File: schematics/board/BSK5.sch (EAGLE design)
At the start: 88 parts, among them U1 STM32F405RGT6, X1 JST-6, X11 JST-6

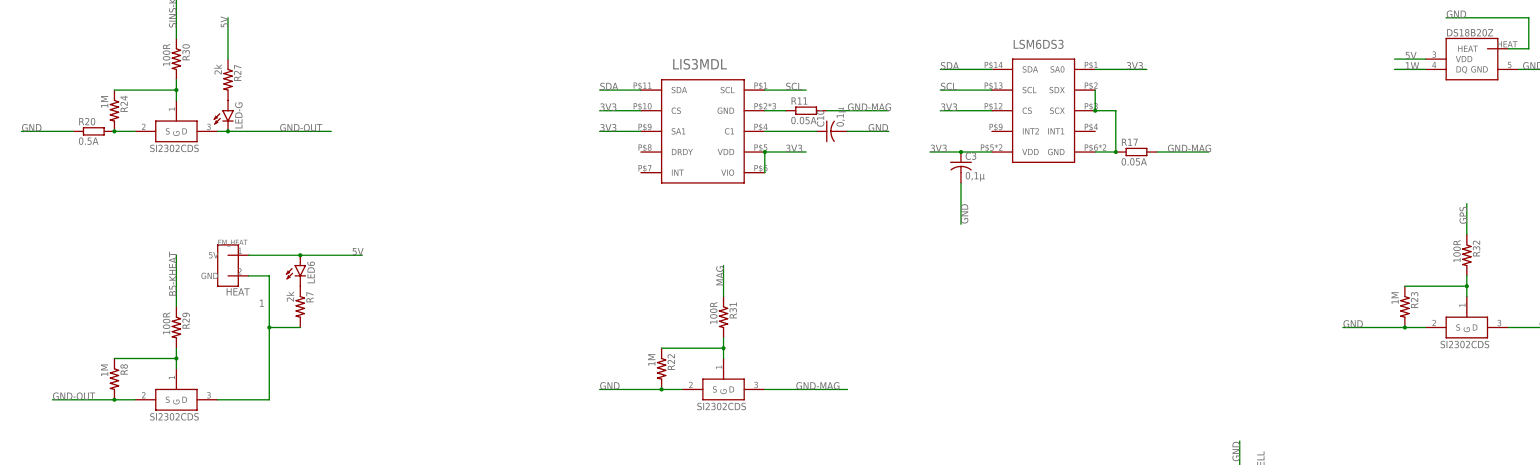
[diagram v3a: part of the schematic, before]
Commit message: На платах БСК устройства по умолчанию подтянуты к питанию
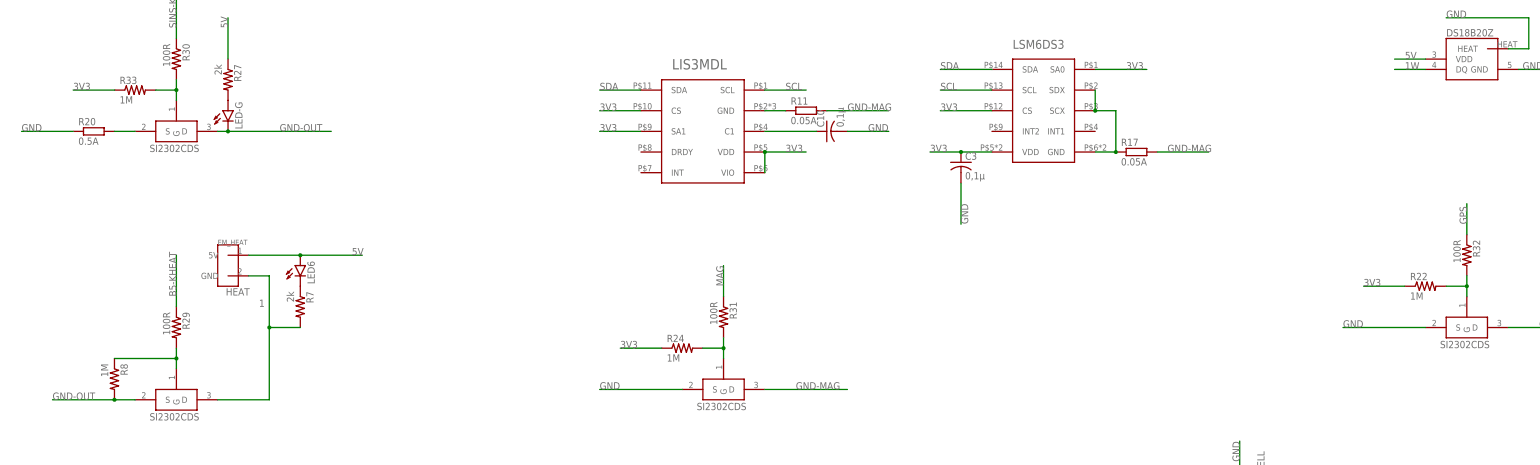
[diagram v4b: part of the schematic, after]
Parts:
- removed R23: 1M, resistor:R-US_R0603
- added R33: 1M, resistor:R-US_R0603
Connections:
- net 11: no longer R24.2
- net 3V3: now also R22.1, R24.1, R33.1
- net GND: no longer R22.2, R23.2
- net N$10: now also R33.2; no longer R24.1
- net N$11: now also R24.2; no longer R22.1
- net N$13: now also R22.2; no longer R23.1
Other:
- moved on the sheet: R22, R24
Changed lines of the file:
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@@
 <part name="R21" library="rcl" library_urn="urn:adsk.eagle:library:334" deviceset="R-EU_" device="R1210" package3d_urn="urn:adsk.eagle:package:23554/2" value="0.2A"/>
 <part name="U$19" library="CanCubeSat" deviceset="SI2302CDS" device=""/>
-<part name="R22" library="resistor" deviceset="R-US_" device="R0603" package3d_urn="urn:adsk.eagle:package:23555/3" value="1M"/>
 <part name="U$20" library="CanCubeSat" deviceset="SI2302CDS" device=""/>
-<part name="R23" library="resistor" deviceset="R-US_" device="R0603" package3d_urn="urn:adsk.eagle:package:23555/3" value="1M"/>
 <part name="U$21" library="CanCubeSat" deviceset="Q24" device=""/>
 <part name="C4" library="rcl" library_urn="urn:adsk.eagle:library:334" deviceset="C-EU" device="C0603" package3d_urn="urn:adsk.eagle:package:23616/2" value="1nF"/>
@@
 <part name="R20" library="rcl" library_urn="urn:adsk.eagle:library:334" deviceset="R-EU_" device="R1210" package3d_urn="urn:adsk.eagle:package:23554/2" value="0.5A"/>
 <part name="U$22" library="CanCubeSat" deviceset="SI2302CDS" device=""/>
-<part name="R24" library="resistor" deviceset="R-US_" device="R0603" package3d_urn="urn:adsk.eagle:package:23555/3" value="1M"/>
 <part name="R27" library="resistor" deviceset="R-US_" device="R0603" package3d_urn="urn:adsk.eagle:package:23555/3" value="2k"/>
 <part name="LED-G" library="led" library_urn="urn:adsk.eagle:library:259" deviceset="LED" device="CHIPLED_0603" package3d_urn="urn:adsk.eagle:package:15822/2"/>
@@
 <part name="R32" library="resistor" deviceset="R-US_" device="R0603" package3d_urn="urn:adsk.eagle:package:23555/3" value="100R"/>
 <part name="U$12" library="CanCubeSat" deviceset="FFC-CONNECT" device="68611"/>
+<part name="R33" library="resistor" deviceset="R-US_" device="R0603" package3d_urn="urn:adsk.eagle:package:23555/3" value="1M"/>
+<part name="R24" library="resistor" deviceset="R-US_" device="R0603" package3d_urn="urn:adsk.eagle:package:23555/3" value="1M"/>
+<part name="R22" library="resistor" deviceset="R-US_" device="R0603" package3d_urn="urn:adsk.eagle:package:23555/3" value="1M"/>
 </parts>
 <sheets>
@@
 </instance>
 <instance part="U$19" gate="G$1" x="340.36" y="269.24" smashed="yes"/>
-<instance part="R22" gate="G$1" x="325.12" y="274.32" smashed="yes" rot="R270">
-<attribute name="NAME" x="326.6186" y="278.13" size="1.778" layer="95" rot="R270"/>
-<attribute name="VALUE" x="321.818" y="278.13" size="1.778" layer="96" rot="R270"/>
-</instance>
 <instance part="U$20" gate="G$1" x="523.24" y="284.48" smashed="yes"/>
-<instance part="R23" gate="G$1" x="508" y="289.56" smashed="yes" rot="R270">
-<attribute name="NAME" x="509.4986" y="293.37" size="1.778" layer="95" rot="R270"/>
-<attribute name="VALUE" x="504.698" y="293.37" size="1.778" layer="96" rot="R270"/>
-</instance>
 <instance part="U$21" gate="G$1" x="533.4" y="111.76" smashed="yes" rot="R180">
 <attribute name="NAME" x="538.48" y="119.38" size="1.778" layer="95" rot="R180"/>
@@
 </instance>
 <instance part="U$22" gate="G$1" x="205.74" y="332.74" smashed="yes"/>
-<instance part="R24" gate="G$1" x="190.5" y="337.82" smashed="yes" rot="R270">
-<attribute name="NAME" x="191.9986" y="341.63" size="1.778" layer="95" rot="R270"/>
-<attribute name="VALUE" x="187.198" y="341.63" size="1.778" layer="96" rot="R270"/>
-</instance>
 <instance part="R27" gate="G$1" x="218.44" y="345.44" smashed="yes" rot="R270">
 <attribute name="NAME" x="219.9386" y="349.25" size="1.778" layer="95" rot="R270"/>
@@
 <attribute name="NAME" x="70.485" y="265.43" size="1.778" layer="95" rot="R90"/>
 <attribute name="VALUE" x="114.3" y="265.43" size="1.778" layer="96" rot="R90"/>
+</instance>
+<instance part="R33" gate="G$1" x="195.58" y="342.9" smashed="yes">
+<attribute name="NAME" x="191.77" y="344.3986" size="1.778" layer="95"/>
+<attribute name="VALUE" x="191.77" y="339.598" size="1.778" layer="96"/>
+</instance>
+<instance part="R24" gate="G$1" x="330.2" y="279.4" smashed="yes">
+<attribute name="NAME" x="326.39" y="280.8986" size="1.778" layer="95"/>
+<attribute name="VALUE" x="326.39" y="276.098" size="1.778" layer="96"/>
+</instance>
+<instance part="R22" gate="G$1" x="513.08" y="294.64" smashed="yes">
+<attribute name="NAME" x="509.27" y="296.1386" size="1.778" layer="95"/>
+<attribute name="VALUE" x="509.27" y="291.338" size="1.778" layer="96"/>
 </instance>
 </instances>
@@
 <segment>
 <pinref part="U$19" gate="G$1" pin="S"/>
-<wire x1="330.2" y1="269.24" x2="325.12" y2="269.24" width="0.1524" layer="91"/>
 <label x="309.88" y="269.24" size="1.778" layer="95"/>
-<pinref part="R22" gate="G$1" pin="2"/>
-<wire x1="325.12" y1="269.24" x2="309.88" y2="269.24" width="0.1524" layer="91"/>
-<junction x="325.12" y="269.24"/>
+<wire x1="330.2" y1="269.24" x2="309.88" y2="269.24" width="0.1524" layer="91"/>
 </segment>
 <segment>
 <pinref part="U$20" gate="G$1" pin="S"/>
-<wire x1="513.08" y1="284.48" x2="508" y2="284.48" width="0.1524" layer="91"/>
 <label x="492.76" y="284.48" size="1.778" layer="95"/>
-<pinref part="R23" gate="G$1" pin="2"/>
-<wire x1="508" y1="284.48" x2="492.76" y2="284.48" width="0.1524" layer="91"/>
-<junction x="508" y="284.48"/>
+<wire x1="513.08" y1="284.48" x2="492.76" y2="284.48" width="0.1524" layer="91"/>
 </segment>
 <segment>
@@
 <wire x1="195.58" y1="332.74" x2="190.5" y2="332.74" width="0.1524" layer="91"/>
 <pinref part="U$22" gate="G$1" pin="S"/>
-<pinref part="R24" gate="G$1" pin="2"/>
 <pinref part="R20" gate="G$1" pin="2"/>
-<junction x="190.5" y="332.74"/>
 </segment>
 </net>
@@
 <label x="73.66" y="248.92" size="1.778" layer="95" rot="R90"/>
 </segment>
+<segment>
+<pinref part="R33" gate="G$1" pin="1"/>
+<wire x1="190.5" y1="342.9" x2="180.34" y2="342.9" width="0.1524" layer="91"/>
+<label x="180.34" y="342.9" size="1.778" layer="95"/>
+</segment>
+<segment>
+<pinref part="R24" gate="G$1" pin="1"/>
+<wire x1="325.12" y1="279.4" x2="314.96" y2="279.4" width="0.1524" layer="91"/>
+<label x="314.96" y="279.4" size="1.778" layer="95"/>
+</segment>
+<segment>
+<pinref part="R22" gate="G$1" pin="1"/>
+<wire x1="508" y1="294.64" x2="497.84" y2="294.64" width="0.1524" layer="91"/>
+<label x="497.84" y="294.64" size="1.778" layer="95"/>
+</segment>
 </net>
 <net name="SINS-KVCC" class="0">
@@
 <pinref part="U$22" gate="G$1" pin="G"/>
 <wire x1="205.74" y1="345.44" x2="205.74" y2="342.9" width="0.1524" layer="91"/>
-<pinref part="R24" gate="G$1" pin="1"/>
+<pinref part="R33" gate="G$1" pin="2"/>
 <wire x1="205.74" y1="342.9" x2="205.74" y2="340.36" width="0.1524" layer="91"/>
-<wire x1="190.5" y1="342.9" x2="205.74" y2="342.9" width="0.1524" layer="91"/>
+<wire x1="200.66" y1="342.9" x2="205.74" y2="342.9" width="0.1524" layer="91"/>
 <junction x="205.74" y="342.9"/>
 </segment>
@@
 <pinref part="U$19" gate="G$1" pin="G"/>
 <wire x1="340.36" y1="281.94" x2="340.36" y2="279.4" width="0.1524" layer="91"/>
-<pinref part="R22" gate="G$1" pin="1"/>
+<pinref part="R24" gate="G$1" pin="2"/>
 <wire x1="340.36" y1="279.4" x2="340.36" y2="276.86" width="0.1524" layer="91"/>
-<wire x1="325.12" y1="279.4" x2="340.36" y2="279.4" width="0.1524" layer="91"/>
+<wire x1="335.28" y1="279.4" x2="340.36" y2="279.4" width="0.1524" layer="91"/>
 <junction x="340.36" y="279.4"/>
 </segment>
@@
 <net name="N$13" class="0">
 <segment>
-<pinref part="R23" gate="G$1" pin="1"/>
-<wire x1="508" y1="294.64" x2="523.24" y2="294.64" width="0.1524" layer="91"/>
 <pinref part="U$20" gate="G$1" pin="G"/>
-<wire x1="523.24" y1="294.64" x2="523.24" y2="292.1" width="0.1524" layer="91"/>
 <pinref part="R32" gate="G$1" pin="2"/>
 <wire x1="523.24" y1="297.18" x2="523.24" y2="294.64" width="0.1524" layer="91"/>
+<pinref part="R22" gate="G$1" pin="2"/>
+<wire x1="523.24" y1="294.64" x2="523.24" y2="292.1" width="0.1524" layer="91"/>
+<wire x1="518.16" y1="294.64" x2="523.24" y2="294.64" width="0.1524" layer="91"/>
 <junction x="523.24" y="294.64"/>
 </segment>

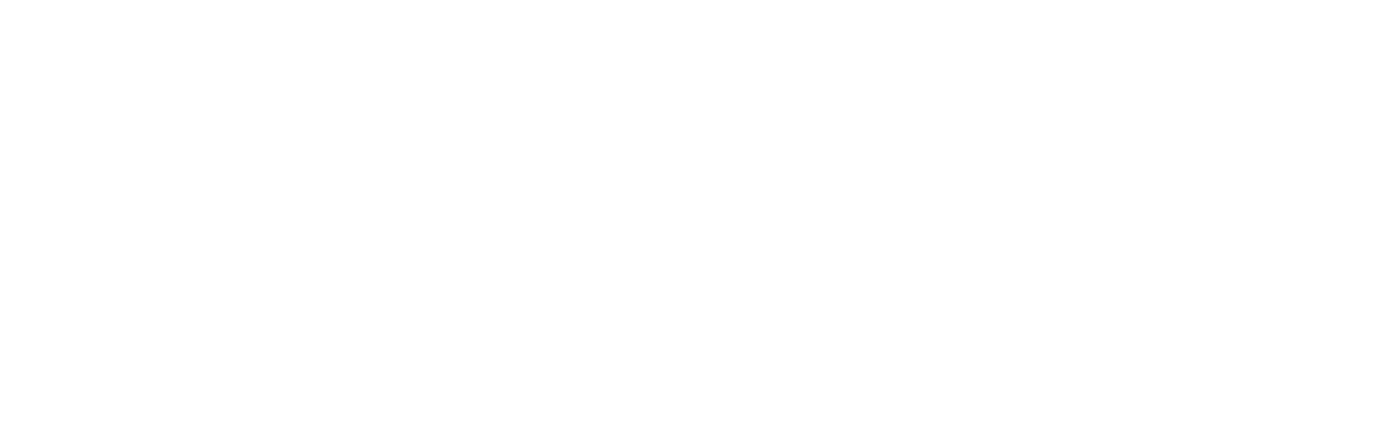
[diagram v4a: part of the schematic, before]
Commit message: Добавлены подписи Концерна к платам
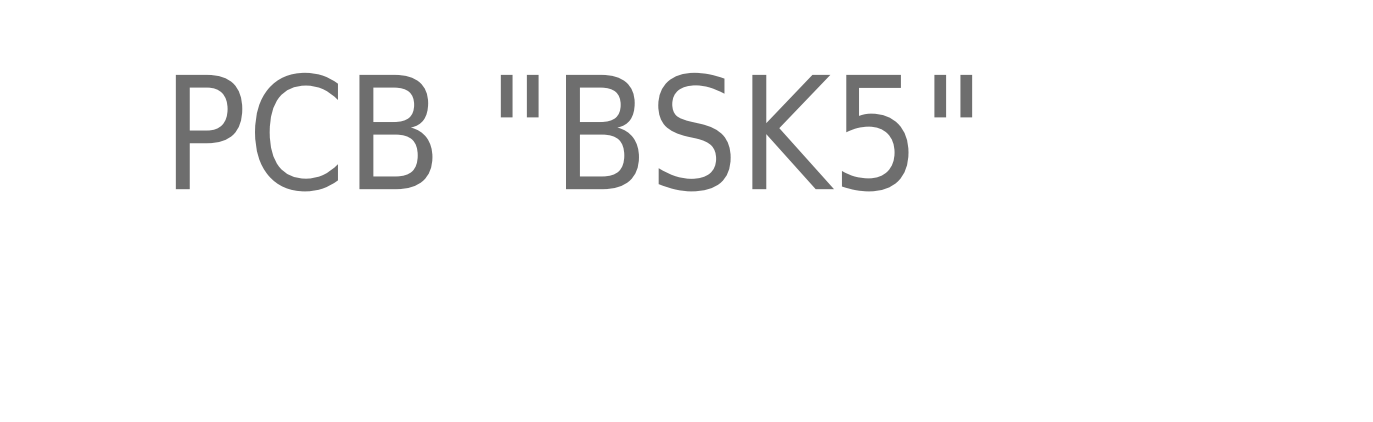
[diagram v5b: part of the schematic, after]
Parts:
- added U$26: PCB "BSK5", CanCubeSat:ITS-LOGOPCB-""
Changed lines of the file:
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@@
 <drawing>
 <settings>
-<setting alwaysvectorfont="no"/>
+<setting alwaysvectorfont="yes"/>
 <setting verticaltext="up"/>
 </settings>
@@
 <part name="R24" library="resistor" deviceset="R-US_" device="R0603" package3d_urn="urn:adsk.eagle:package:23555/3" value="1M"/>
 <part name="R22" library="resistor" deviceset="R-US_" device="R0603" package3d_urn="urn:adsk.eagle:package:23555/3" value="1M"/>
+<part name="U$26" library="CanCubeSat" deviceset="ITS-LOGO" device="PCB-&quot;&quot;" value="PCB &quot;BSK5&quot;"/>
 </parts>
 <sheets>
@@
 <attribute name="VALUE" x="509.27" y="291.338" size="1.778" layer="96"/>
 </instance>
+<instance part="U$26" gate="G$1" x="182.88" y="434.34" smashed="yes">
+<attribute name="VALUE" x="309.88" y="434.34" size="12.7" layer="96"/>
+</instance>
 </instances>

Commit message: Начато исправление разъемов
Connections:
- net RX-S: now also U1.PC11; no longer U1.PC10
- net TX-S: now also U1.PC10; no longer U1.PC11
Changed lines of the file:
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@@
 <net name="RX-S" class="0">
+<segment>
+<wire x1="81.28" y1="269.24" x2="81.28" y2="248.92" width="0.1524" layer="91"/>
+<label x="81.28" y="248.92" size="1.778" layer="95" rot="R90"/>
+<pinref part="U$12" gate="G$1" pin="4"/>
+</segment>
+<segment>
+<pinref part="U1" gate="G$1" pin="PC11"/>
+<wire x1="482.6" y1="154.94" x2="492.76" y2="154.94" width="0.1524" layer="91"/>
+<label x="487.68" y="154.94" size="1.778" layer="95"/>
+</segment>
+</net>
+<net name="TX-S" class="0">
+<segment>
+<wire x1="86.36" y1="269.24" x2="86.36" y2="248.92" width="0.1524" layer="91"/>
+<label x="86.36" y="248.92" size="1.778" layer="95" rot="R90"/>
+<pinref part="U$12" gate="G$1" pin="6"/>
+</segment>
 <segment>
 <pinref part="U1" gate="G$1" pin="PC10"/>
@@
 <label x="487.68" y="157.48" size="1.778" layer="95"/>
 </segment>
-<segment>
-<wire x1="81.28" y1="269.24" x2="81.28" y2="248.92" width="0.1524" layer="91"/>
-<label x="81.28" y="248.92" size="1.778" layer="95" rot="R90"/>
-<pinref part="U$12" gate="G$1" pin="4"/>
-</segment>
 </net>
-<net name="TX-S" class="0">
-<segment>
-<pinref part="U1" gate="G$1" pin="PC11"/>
-<wire x1="482.6" y1="154.94" x2="492.76" y2="154.94" width="0.1524" layer="91"/>
-<label x="487.68" y="154.94" size="1.778" layer="95"/>
-</segment>
-<segment>
-<wire x1="86.36" y1="269.24" x2="86.36" y2="248.92" width="0.1524" layer="91"/>
-<label x="86.36" y="248.92" size="1.778" layer="95" rot="R90"/>
-<pinref part="U$12" gate="G$1" pin="6"/>
-</segment>
-</net>

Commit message: Плата BSK5 на проверку
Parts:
- removed C53: 100nF, rcl:C-EUC0603
- removed LED-G: (no value), led:LEDCHIPLED_0603
- removed LIS3MDL: LIS3MDL, CanCubeSat:LIS3MDL
- removed LSM6DS3: LSM6DS3, CanCubeSat:LSM6DS3
- removed R11, R17: 0.05A, rcl:R-EU_R1210
- removed R27: 2k, resistor:R-US_R0603
- added C21: 1uF, CanCubeSat:ECAP1UF
- added LIS3MDL-GY: LIS3MDL-GY, CanCubeSat:LIS3MDL-GY
- added LSM6DS3-GY: LSM6DS3-GY, CanCubeSat:LSM6DS3-GY
- added R23, R34: 0.05A, rcl:R-EU_R1210
- added STAB: ADP150AUJZ-3.3-R7, CanCubeSat:ADP150AUJZ-3.3-R7
- C10: value 0,1µ -> 1uF; device rcl:C-USC0603 -> CanCubeSat:ECAP1UF
- C3: value 0,1µ -> 100nF; device rcl:C-USC0603 -> rcl:C-EUC0603
- X1, X11: value JST-6 -> JST-6A; device CanCubeSat:JST-6 -> CanCubeSat:JST-6A
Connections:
- removed net 11: R20.2, U$22.S
- removed net N$8: LSM6DS3.GND, LSM6DS3.SCX, LSM6DS3.SDX, R17.1
- removed net N$9: LED-G.A, R27.2
- new net N$12: LSM6DS3-GY.GND, LSM6DS3-GY.SCX, LSM6DS3-GY.SDX, R23.1
- new net N$14: LIS3MDL-GY.GND, R34.1
- net 3V3: now also LIS3MDL-GY.3V3, LSM6DS3-GY.3V3; no longer C3.1, C53.2, LIS3MDL.CS, LIS3MDL.SA1, LIS3MDL.VDD, LIS3MDL.VIO, LSM6DS3.CS, LSM6DS3.SA0, LSM6DS3.VDD, U1.VDDA
- net 5V: now also C21.1, STAB.EN, STAB.VIN; no longer R27.1
- net GND: now also C21.2, R20.2, STAB.GND; no longer C53.1, R20.1
- net GND-MAG: now also R23.2, R34.2; no longer R11.2, R17.2
- net GND-OUT: now also U$22.S; no longer LED-G.C, U$22.D
- net N$2: now also R20.1, U$22.D; no longer LIS3MDL.GND, R11.1
- net N$3: now also C3.1, STAB.VOUT, U1.VDDA; no longer LIS3MDL.C1
- net SCL: now also LIS3MDL-GY.SCL, LSM6DS3-GY.SCL; no longer LIS3MDL.SCL, LSM6DS3.SCL
- net SDA: now also LIS3MDL-GY.SDA, LSM6DS3-GY.SDA; no longer LIS3MDL.SDA, LSM6DS3.SDA
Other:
- moved on the sheet: BT1, C10, C3, D1, R10, R20

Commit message: Исправлена БСК5
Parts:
- removed C10, C21: 1uF, CanCubeSat:ECAP1UF
- removed STAB: ADP150AUJZ-3.3-R7, CanCubeSat:ADP150AUJZ-3.3-R7
- added U$6: REF3033, CanCubeSat:REF3033
- C3: value 100nF -> 470nF
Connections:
- removed net N$3: C10.1, C3.1, STAB.VOUT, U1.VDDA
- new net 3V3-STAB: C11.1, C12.1, C14.1, C15.1, C16.1, C17.1, C2.1, C6.1, C7.1, C8.1, U$1.V+, U$10.V+, U$11.V+, U$2.V+, U$23.V+, U$3.V+, U$4.V+, U$5.V+, U$6.OUT, U$7.V+, U$9.V+, U1.VDDA
- net 5V: now also C3.2, U$6.IN; no longer C11.1, C12.1, C14.1, C15.1, C16.1, C17.1, C2.1, C21.1, C6.1, C7.1, C8.1, STAB.EN, STAB.VIN, U$1.V+, U$10.V+, U$11.V+, U$2.V+, U$23.V+, U$3.V+, U$4.V+, U$5.V+, U$7.V+, U$9.V+
- net GND: now also C3.1, U$6.GND; no longer C10.2, C21.2, C3.2, STAB.GND
- net SS4: now also U1.PC2/SPI2_MISO; no longer U1.PA6/SPI1_MISO
- net TIME-ES: now also U1.PA6/SPI1_MISO; no longer U1.PA9
- net TIME-G: now also U1.PA7/SPI1_MOSI; no longer U1.PA10
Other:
- moved on the sheet: C11, C12, C14, C15, C16, C17, C2, C3, C6, C7, C8, R12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
